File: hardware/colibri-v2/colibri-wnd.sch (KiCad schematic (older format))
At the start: 0 parts

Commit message: Assigning footprints
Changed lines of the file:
@@
 F12 "BOOT0" O R 5350 5900 60
 F13 "MODULE_RESET#" O R 5350 7000 60
+F14 "LED0" I R 5350 6900 60
 $EndSheet
 $Sheet
@@
 F107 "FMC_SDNE0" O R 11250 7450 60
 F108 "PWM_SRV_EN" O R 11250 4900 60
+F109 "LED0" O L 7000 6900 60
 $EndSheet
 $Sheet
@@
 Wire Wire Line
 	11250 4900 12700 4900
+Wire Wire Line
+	7000 6900 5350 6900
 $EndSCHEMATC

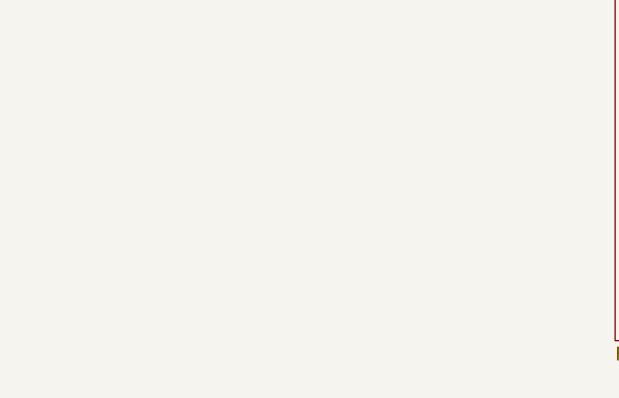
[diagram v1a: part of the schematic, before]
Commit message: Added STANDOFF-4-40.kicad_mod footprint
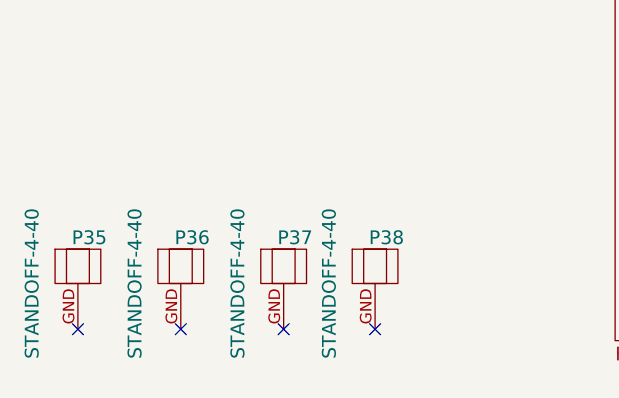
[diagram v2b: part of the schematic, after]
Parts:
- added P35, P36, P37, P38: STANDOFF-4-40, Sigmadrone:STANDOFF-4-40, symbol STANDOFF-4-40
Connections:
- no-connect marks 0 -> 4
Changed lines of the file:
@@
 Wire Wire Line
 	7000 6900 5350 6900
+$Comp
+L STANDOFF-4-40 P35
+U 1 1 56D94983
+P 1150 9700
+F 0 "P35" H 1200 9900 60  0000 C CNN
+F 1 "STANDOFF-4-40" V 950 9700 60  0000 C CNN
+F 2 "Sigmadrone:STANDOFF-4-40" H 1150 9300 60  0001 C CNN
+F 3 "" H 1150 9700 60  0000 C CNN
+	1    1150 9700
+	1    0    0    -1
+$EndComp
+$Comp
+L STANDOFF-4-40 P36
+U 1 1 56D95F62
+P 1600 9700
+F 0 "P36" H 1650 9900 60  0000 C CNN
+F 1 "STANDOFF-4-40" V 1400 9700 60  0000 C CNN
+F 2 "Sigmadrone:STANDOFF-4-40" H 1600 9300 60  0001 C CNN
+F 3 "" H 1600 9700 60  0000 C CNN
+	1    1600 9700
+	1    0    0    -1
+$EndComp
+$Comp
+L STANDOFF-4-40 P37
+U 1 1 56D964DE
+P 2050 9700
+F 0 "P37" H 2100 9900 60  0000 C CNN
+F 1 "STANDOFF-4-40" V 1850 9700 60  0000 C CNN
+F 2 "Sigmadrone:STANDOFF-4-40" H 2050 9300 60  0001 C CNN
+F 3 "" H 2050 9700 60  0000 C CNN
+	1    2050 9700
+	1    0    0    -1
+$EndComp
+$Comp
+L STANDOFF-4-40 P38
+U 1 1 56D96A5F
+P 2450 9700
+F 0 "P38" H 2500 9900 60  0000 C CNN
+F 1 "STANDOFF-4-40" V 2250 9700 60  0000 C CNN
+F 2 "Sigmadrone:STANDOFF-4-40" H 2450 9300 60  0001 C CNN
+F 3 "" H 2450 9700 60  0000 C CNN
+	1    2450 9700
+	1    0    0    -1
+$EndComp
+NoConn ~ 1150 9900
+NoConn ~ 1600 9900
+NoConn ~ 2050 9900
+NoConn ~ 2450 9900
 $EndSCHEMATC

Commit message: Work on PCB placement
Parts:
- removed P35, P36, P37, P38: STANDOFF-4-40, Sigmadrone:STANDOFF-4-40, symbol STANDOFF-4-40
- added P35, P36, P37, P38: STANDOFF, Sigmadrone:STANDOFF-6-32, symbol STANDOFF
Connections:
- new net GND: P35.GND, P36.GND, P37.GND, P38.GND
- no-connect marks 4 -> 0
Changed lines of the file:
@@
 Wire Wire Line
 	7000 6900 5350 6900
+Wire Wire Line
+	1150 9900 1150 10150
+Wire Wire Line
+	1150 10150 2450 10150
+Wire Wire Line
+	2450 10150 2450 9900
+Wire Wire Line
+	2050 9900 2050 10150
+Connection ~ 2050 10150
+Wire Wire Line
+	1600 9900 1600 10650
+Connection ~ 1600 10150
 $Comp
-L STANDOFF-4-40 P35
-U 1 1 56D94983
+L GND #PWR01
+U 1 1 56D9B103
+P 1600 10650
+F 0 "#PWR01" H 1600 10400 50  0001 C CNN
+F 1 "GND" H 1600 10500 50  0000 C CNN
+F 2 "" H 1600 10650 50  0000 C CNN
+F 3 "" H 1600 10650 50  0000 C CNN
+	1    1600 10650
+	1    0    0    -1
+$EndComp
+$Comp
+L STANDOFF P35
+U 1 1 56DAC68C
 P 1150 9700
 F 0 "P35" H 1200 9900 60  0000 C CNN
-F 1 "STANDOFF-4-40" V 950 9700 60  0000 C CNN
-F 2 "Sigmadrone:STANDOFF-4-40" H 1150 9300 60  0001 C CNN
+F 1 "STANDOFF" V 1000 9750 60  0000 C CNN
+F 2 "Sigmadrone:STANDOFF-6-32" H 1150 9300 60  0001 C CNN
 F 3 "" H 1150 9700 60  0000 C CNN
 	1    1150 9700
@@
 $EndComp
 $Comp
-L STANDOFF-4-40 P36
-U 1 1 56D95F62
-P 1600 9700
-F 0 "P36" H 1650 9900 60  0000 C CNN
-F 1 "STANDOFF-4-40" V 1400 9700 60  0000 C CNN
-F 2 "Sigmadrone:STANDOFF-4-40" H 1600 9300 60  0001 C CNN
-F 3 "" H 1600 9700 60  0000 C CNN
-	1    1600 9700
+L STANDOFF P38
+U 1 1 56DADC7C
+P 2450 9700
+F 0 "P38" H 2500 9900 60  0000 C CNN
+F 1 "STANDOFF" V 2300 9750 60  0000 C CNN
+F 2 "Sigmadrone:STANDOFF-6-32" H 2450 9300 60  0001 C CNN
+F 3 "" H 2450 9700 60  0000 C CNN
+	1    2450 9700
 	1    0    0    -1
 $EndComp
 $Comp
-L STANDOFF-4-40 P37
-U 1 1 56D964DE
+L STANDOFF P37
+U 1 1 56DAD6FD
 P 2050 9700
 F 0 "P37" H 2100 9900 60  0000 C CNN
-F 1 "STANDOFF-4-40" V 1850 9700 60  0000 C CNN
-F 2 "Sigmadrone:STANDOFF-4-40" H 2050 9300 60  0001 C CNN
+F 1 "STANDOFF" V 1900 9750 60  0000 C CNN
+F 2 "Sigmadrone:STANDOFF-6-32" H 2050 9300 60  0001 C CNN
 F 3 "" H 2050 9700 60  0000 C CNN
 	1    2050 9700
@@
 $EndComp
 $Comp
-L STANDOFF-4-40 P38
-U 1 1 56D96A5F
-P 2450 9700
-F 0 "P38" H 2500 9900 60  0000 C CNN
-F 1 "STANDOFF-4-40" V 2250 9700 60  0000 C CNN
-F 2 "Sigmadrone:STANDOFF-4-40" H 2450 9300 60  0001 C CNN
-F 3 "" H 2450 9700 60  0000 C CNN
-	1    2450 9700
+L STANDOFF P36
+U 1 1 56DAD179
+P 1600 9700
+F 0 "P36" H 1650 9900 60  0000 C CNN
+F 1 "STANDOFF" V 1450 9750 60  0000 C CNN
+F 2 "Sigmadrone:STANDOFF-6-32" H 1600 9300 60  0001 C CNN
+F 3 "" H 1600 9700 60  0000 C CNN
+	1    1600 9700
 	1    0    0    -1
 $EndComp
-NoConn ~ 1150 9900
-NoConn ~ 1600 9900
-NoConn ~ 2050 9900
-NoConn ~ 2450 9900
 $EndSCHEMATC

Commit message: Working on placement.
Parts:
- added P?: STANDOFF, Sigmadrone:STANDOFF-6-32, symbol STANDOFF
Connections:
- net GND: now also P?.GND
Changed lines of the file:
@@
 	1150 9900 1150 10150
 Wire Wire Line
-	1150 10150 2450 10150
+	1150 10150 2950 10150
 Wire Wire Line
 	2450 10150 2450 9900
@@
 	1    0    0    -1
 $EndComp
+$Comp
+L STANDOFF P?
+U 1 1 56DBAB81
+P 2950 9700
+F 0 "P?" H 3000 9900 60  0000 C CNN
+F 1 "STANDOFF" V 2800 9750 60  0000 C CNN
+F 2 "Sigmadrone:STANDOFF-6-32" H 2950 9300 60  0001 C CNN
+F 3 "" H 2950 9700 60  0000 C CNN
+	1    2950 9700
+	1    0    0    -1
+$EndComp
+Wire Wire Line
+	2950 10150 2950 9900
+Connection ~ 2450 10150
 $EndSCHEMATC

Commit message: Work on placement
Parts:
- gave numbers to parts that had none: 1
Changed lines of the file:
@@
 $EndComp
 $Comp
-L STANDOFF P?
+L STANDOFF P39
 U 1 1 56DBAB81
 P 2950 9700
-F 0 "P?" H 3000 9900 60  0000 C CNN
+F 0 "P39" H 3000 9900 60  0000 C CNN
 F 1 "STANDOFF" V 2800 9750 60  0000 C CNN
 F 2 "Sigmadrone:STANDOFF-6-32" H 2950 9300 60  0001 C CNN

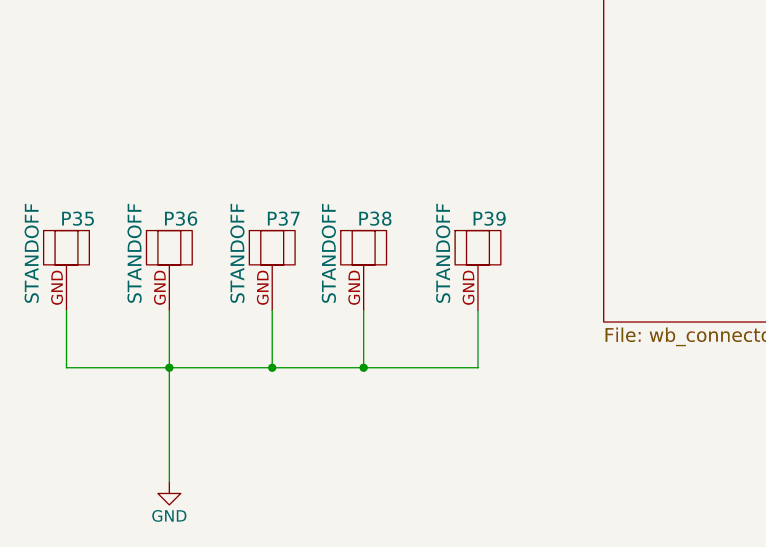
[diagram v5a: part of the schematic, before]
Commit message: Added one more standoff, next to external sensors
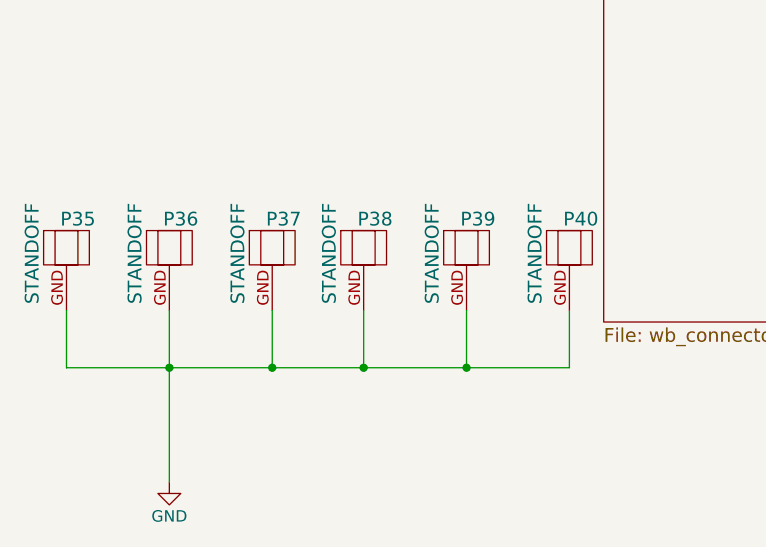
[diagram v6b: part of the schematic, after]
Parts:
- added P40: STANDOFF, Sigmadrone:STANDOFF-6-32, symbol STANDOFF
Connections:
- net GND: now also P40.GND
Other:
- moved on the sheet: P39
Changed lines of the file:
@@
 	1150 9900 1150 10150
 Wire Wire Line
-	1150 10150 2950 10150
+	1150 10150 3350 10150
 Wire Wire Line
 	2450 10150 2450 9900
@@
 L STANDOFF P39
 U 1 1 56DBAB81
-P 2950 9700
-F 0 "P39" H 3000 9900 60  0000 C CNN
-F 1 "STANDOFF" V 2800 9750 60  0000 C CNN
-F 2 "Sigmadrone:STANDOFF-6-32" H 2950 9300 60  0001 C CNN
-F 3 "" H 2950 9700 60  0000 C CNN
-	1    2950 9700
+P 2900 9700
+F 0 "P39" H 2950 9900 60  0000 C CNN
+F 1 "STANDOFF" V 2750 9750 60  0000 C CNN
+F 2 "Sigmadrone:STANDOFF-6-32" H 2900 9300 60  0001 C CNN
+F 3 "" H 2900 9700 60  0000 C CNN
+	1    2900 9700
 	1    0    0    -1
 $EndComp
 Wire Wire Line
-	2950 10150 2950 9900
+	2900 10150 2900 9900
 Connection ~ 2450 10150
+$Comp
+L STANDOFF P40
+U 1 1 56E525E3
+P 3350 9700
+F 0 "P40" H 3400 9900 60  0000 C CNN
+F 1 "STANDOFF" V 3200 9750 60  0000 C CNN
+F 2 "Sigmadrone:STANDOFF-6-32" H 3350 9300 60  0001 C CNN
+F 3 "" H 3350 9700 60  0000 C CNN
+	1    3350 9700
+	1    0    0    -1
+$EndComp
+Wire Wire Line
+	3350 10150 3350 9900
+Connection ~ 2900 10150
 $EndSCHEMATC

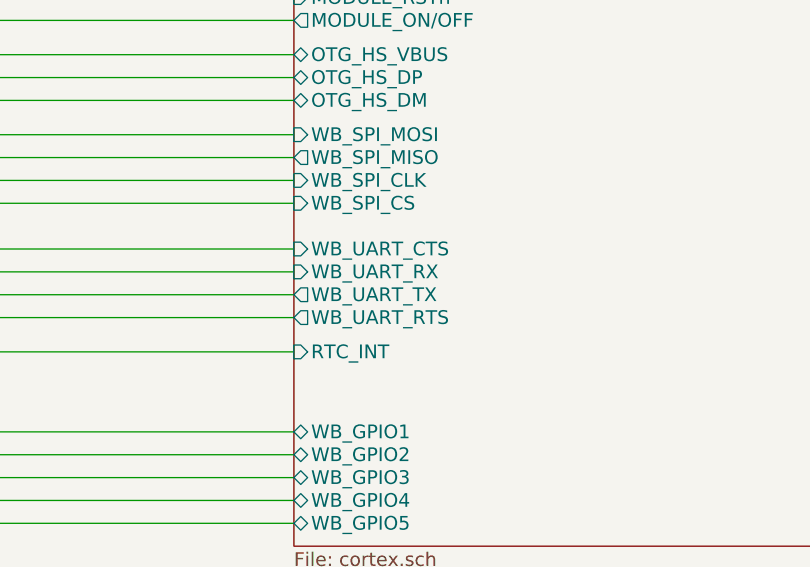
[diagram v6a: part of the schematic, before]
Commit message: Redefined the labels for the inter boards UART communication.
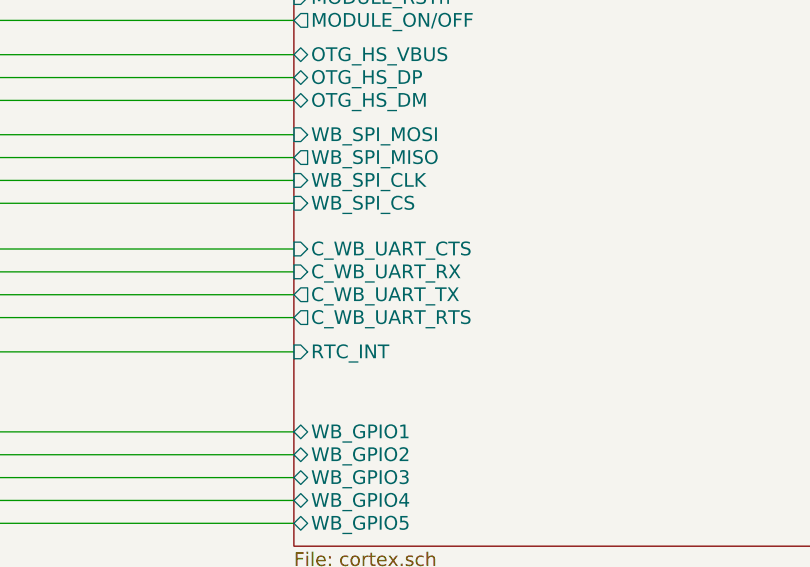
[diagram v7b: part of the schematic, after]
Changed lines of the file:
@@
 F52 "MEMS_ACC_CS" O L 7000 1850 60
 F53 "IN_PWM_03" I R 11250 5600 60
-F54 "WB_UART_RX" I L 7000 8750 60
-F55 "WB_UART_TX" O L 7000 8850 60
-F56 "WB_UART_RTS" O L 7000 8950 60
-F57 "WB_UART_CTS" I L 7000 8650 60
-F58 "WB_SPI_CLK" I L 7000 8350 60
-F59 "WB_SPI_CS" I L 7000 8450 60
-F60 "BUTTON_4" I L 7000 6400 60
-F61 "RTC_INT" I L 7000 9100 60
-F62 "SRV_PWM_2" O R 11250 4250 60
-F63 "SRV_PWM_1" O R 11250 4150 60
-F64 "WB_SPI_MISO" O L 7000 8250 60
-F65 "WB_SPI_MOSI" I L 7000 8150 60
-F66 "LED1" O L 7000 6500 60
-F67 "LED2" O L 7000 6600 60
-F68 "LED3" O L 7000 6700 60
-F69 "LED4" O L 7000 6800 60
-F70 "WB_GPIO1" B L 7000 9450 60
-F71 "WB_GPIO2" B L 7000 9550 60
-F72 "WB_GPIO3" B L 7000 9650 60
-F73 "WB_GPIO4" B L 7000 9750 60
-F74 "WB_GPIO5" B L 7000 9850 60
-F75 "MSRMNT_ON" O L 7000 4200 60
-F76 "PWR_BTN_READ" I L 7000 3900 60
-F77 "PWR_ON" O L 7000 4300 60
-F78 "C_I2C2_SCL" O R 11250 8800 60
-F79 "C_I2C2_SDA" B R 11250 8900 60
-F80 "C_I2C3_SCL" O R 11250 9050 60
-F81 "C_I2C3_SDA" B R 11250 9150 60
-F82 "FMC_SDNWE" O R 11250 7750 60
-F83 "FMC_NBL[0..1]" B R 11250 7050 60
-F84 "FMC_SDNRAS" O R 11250 7550 60
-F85 "FMC_BA[0..1]" B R 11250 6950 60
-F86 "FMC_SDCLK" O R 11250 7850 60
-F87 "FMC_SDNCAS" O R 11250 7650 60
-F88 "FMC_A[0..11]" O R 11250 7250 60
-F89 "FMC_D[0..15]" B R 11250 7150 60
-F90 "MEMS_SPI5_SCK" O L 7000 2050 60
-F91 "MEMS_SPI5_MISO" I L 7000 2250 60
-F92 "MEMS_SPI5_MOSI" O L 7000 2150 60
-F93 "MEMS_ACC_INT1" I L 7000 2650 60
-F94 "C_SPI2_NSS1" O R 11250 8250 60
-F95 "C_SPI2_SCK" O R 11250 8450 60
-F96 "C_SPI2_MISO" I R 11250 8550 60
-F97 "C_SPI2_MOSI" O R 11250 8650 60
-F98 "C_SPI2_NSS2" O R 11250 8350 60
-F99 "EXT_GPIO_1" B R 11250 9300 60
-F100 "EXT_GPIO_2" B R 11250 9400 60
-F101 "EXT_GPIO_3" B R 11250 9500 60
-F102 "EXT_GPIO_4" B R 11250 9600 60
-F103 "EXT_GPIO_5" B R 11250 9700 60
-F104 "EXT_GPIO_6" B R 11250 9800 60
-F105 "GPS_PWR_CTRL" O R 11250 3350 60
-F106 "FMC_SDCKE0" O R 11250 7350 60
-F107 "FMC_SDNE0" O R 11250 7450 60
-F108 "PWM_SRV_EN" O R 11250 4900 60
-F109 "LED0" O L 7000 6900 60
+F54 "WB_SPI_CLK" I L 7000 8350 60
+F55 "WB_SPI_CS" I L 7000 8450 60
+F56 "BUTTON_4" I L 7000 6400 60
+F57 "RTC_INT" I L 7000 9100 60
+F58 "SRV_PWM_2" O R 11250 4250 60
+F59 "SRV_PWM_1" O R 11250 4150 60
+F60 "WB_SPI_MISO" O L 7000 8250 60
+F61 "WB_SPI_MOSI" I L 7000 8150 60
+F62 "LED1" O L 7000 6500 60
+F63 "LED2" O L 7000 6600 60
+F64 "LED3" O L 7000 6700 60
+F65 "LED4" O L 7000 6800 60
+F66 "WB_GPIO1" B L 7000 9450 60
+F67 "WB_GPIO2" B L 7000 9550 60
+F68 "WB_GPIO3" B L 7000 9650 60
+F69 "WB_GPIO4" B L 7000 9750 60
+F70 "WB_GPIO5" B L 7000 9850 60
+F71 "MSRMNT_ON" O L 7000 4200 60
+F72 "PWR_BTN_READ" I L 7000 3900 60
+F73 "PWR_ON" O L 7000 4300 60
+F74 "C_I2C2_SCL" O R 11250 8800 60
+F75 "C_I2C2_SDA" B R 11250 8900 60
+F76 "C_I2C3_SCL" O R 11250 9050 60
+F77 "C_I2C3_SDA" B R 11250 9150 60
+F78 "FMC_SDNWE" O R 11250 7750 60
+F79 "FMC_NBL[0..1]" B R 11250 7050 60
+F80 "FMC_SDNRAS" O R 11250 7550 60
+F81 "FMC_BA[0..1]" B R 11250 6950 60
+F82 "FMC_SDCLK" O R 11250 7850 60
+F83 "FMC_SDNCAS" O R 11250 7650 60
+F84 "FMC_A[0..11]" O R 11250 7250 60
+F85 "FMC_D[0..15]" B R 11250 7150 60
+F86 "MEMS_SPI5_SCK" O L 7000 2050 60
+F87 "MEMS_SPI5_MISO" I L 7000 2250 60
+F88 "MEMS_SPI5_MOSI" O L 7000 2150 60
+F89 "MEMS_ACC_INT1" I L 7000 2650 60
+F90 "C_SPI2_NSS1" O R 11250 8250 60
+F91 "C_SPI2_SCK" O R 11250 8450 60
+F92 "C_SPI2_MISO" I R 11250 8550 60
+F93 "C_SPI2_MOSI" O R 11250 8650 60
+F94 "C_SPI2_NSS2" O R 11250 8350 60
+F95 "EXT_GPIO_1" B R 11250 9300 60
+F96 "EXT_GPIO_2" B R 11250 9400 60
+F97 "EXT_GPIO_3" B R 11250 9500 60
+F98 "EXT_GPIO_4" B R 11250 9600 60
+F99 "EXT_GPIO_5" B R 11250 9700 60
+F100 "EXT_GPIO_6" B R 11250 9800 60
+F101 "GPS_PWR_CTRL" O R 11250 3350 60
+F102 "FMC_SDCKE0" O R 11250 7350 60
+F103 "FMC_SDNE0" O R 11250 7450 60
+F104 "PWM_SRV_EN" O R 11250 4900 60
+F105 "LED0" O L 7000 6900 60
+F106 "C_WB_UART_RX" I L 7000 8750 60
+F107 "C_WB_UART_TX" O L 7000 8850 60
+F108 "C_WB_UART_RTS" O L 7000 8950 60
+F109 "C_WB_UART_CTS" I L 7000 8650 60
 $EndSheet
 $Sheet
